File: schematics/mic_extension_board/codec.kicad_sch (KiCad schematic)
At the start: 26 parts, among them J10 Conn_01x01_Female, J11 Conn_01x01_Female, U6 CS4270-CZZ, X1 SG-5032CAN

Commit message: finished full board
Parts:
- C10, C12, C20: value 10uF -> C_Polarized
- C11, C13, C18, C21, C22: value 0.1uF -> C
- C14, C15: value 220pF -> C
- C16, C17: value 3.3uF -> C_Polarized
- C19: value 47uF -> C_Polarized
- C23, C24: value 3.3nF -> C
- R10, R9: value 470 -> R
- R19, R20: value 2k2 -> R
- R6: value 47k -> R
- R7, R8: value 10k -> R
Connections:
- net 3V3: now reaches C11.1, C13.1, R19.2, R20.2, U6.5 (VD), U6.8 (VLC), X1.4 (VCC)
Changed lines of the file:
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@@
   (junction (at 83.82 97.79) (diameter 0) (color 0 0 0 0)
   )
+  (junction (at 86.36 39.37) (diameter 0) (color 0 0 0 0)
+  )
   (junction (at 102.87 74.93) (diameter 0) (color 0 0 0 0)
   )
@@
     (stroke (width 0) (type default))
   )
+  (wire (pts (xy 86.36 39.37) (xy 82.55 39.37))
+    (stroke (width 0) (type default))
+  )
   (wire (pts (xy 95.25 85.09) (xy 99.06 85.09))
     (stroke (width 0) (type default))
@@
     (stroke (width 0) (type default))
   )
-  (wire (pts (xy 97.79 39.37) (xy 82.55 39.37))
+  (wire (pts (xy 97.79 39.37) (xy 86.36 39.37))
     (stroke (width 0) (type default))
   )
@@
     (stroke (width 0) (type default))
   )
+  (wire (pts (xy 86.36 36.83) (xy 86.36 39.37))
+    (stroke (width 0) (type default))
+  )
   (wire (pts (xy 144.78 116.84) (xy 214.63 116.84))
     (stroke (width 0) (type default))
@@
   (wire (pts (xy 90.17 82.55) (xy 99.06 82.55))
     (stroke (width 0) (type default))
+  )
+  (global_label "3V3" (shape input) (at 86.36 36.83 90) (fields_autoplaced)
+    (effects (font (size 1.27 1.27)) (justify left))
+    (property "Intersheetrefs" "${INTERSHEET_REFS}" (at 86.36 30.3372 90)
+      (effects (font (size 1.27 1.27)) (justify left) hide)
+    )
   )
   (global_label "5V" (shape input) (at 186.69 114.3 0) (fields_autoplaced)
@@
       (effects (font (size 1.27 1.27)))
     )
-    (property "Value" "470" (at 203.2 49.53 90)
+    (property "Value" "R" (at 203.2 49.53 90)
       (effects (font (size 1.27 1.27)))
     )
@@
       (effects (font (size 1.27 1.27)))
     )
-    (property "Value" "47uF" (at 191.77 92.71 90)
+    (property "Value" "C_Polarized" (at 191.77 92.71 90)
       (effects (font (size 1.27 1.27)))
     )
@@
       (effects (font (size 1.27 1.27)))
     )
-    (property "Value" "220pF" (at 111.76 97.79 90)
+    (property "Value" "C" (at 111.76 97.79 90)
       (effects (font (size 1.27 1.27)))
     )
@@
       (effects (font (size 1.27 1.27)))
     )
-    (property "Value" "10k" (at 191.77 52.07 90)
+    (property "Value" "R" (at 191.77 52.07 90)
       (effects (font (size 1.27 1.27)))
     )
@@
       (effects (font (size 1.27 1.27)))
     )
-    (property "Value" "3.3nF" (at 209.55 54.61 90)
+    (property "Value" "C" (at 209.55 54.61 90)
       (effects (font (size 1.27 1.27)))
     )
@@
       (effects (font (size 1.27 1.27)))
     )
-    (property "Value" "0.1uF" (at 189.23 102.87 90)
+    (property "Value" "C" (at 189.23 102.87 90)
       (effects (font (size 1.27 1.27)))
     )
@@
       (effects (font (size 1.27 1.27)))
     )
-    (property "Value" "3.3uF" (at 181.61 48.26 90)
+    (property "Value" "C_Polarized" (at 181.61 48.26 90)
       (effects (font (size 1.27 1.27)))
     )
@@
       (effects (font (size 1.27 1.27)))
     )
-    (property "Value" "2k2" (at 111.76 114.3 90)
+    (property "Value" "R" (at 111.76 114.3 90)
       (effects (font (size 1.27 1.27)))
     )
@@
       (effects (font (size 1.27 1.27)))
     )
-    (property "Value" "0.1uF" (at 207.01 88.9 90)
+    (property "Value" "C" (at 207.01 88.9 90)
       (effects (font (size 1.27 1.27)))
     )
@@
       (effects (font (size 1.27 1.27)))
     )
-    (property "Value" "10uF" (at 101.6 91.44 90)
+    (property "Value" "C_Polarized" (at 101.6 91.44 90)
       (effects (font (size 1.27 1.27)))
     )
@@
       (effects (font (size 1.27 1.27)))
     )
-    (property "Value" "0.1uF" (at 95.25 76.2 0)
+    (property "Value" "C" (at 95.25 76.2 0)
       (effects (font (size 1.27 1.27)))
     )
@@
       (effects (font (size 1.27 1.27)))
     )
-    (property "Value" "0.1uF" (at 207.01 96.52 90)
+    (property "Value" "C" (at 207.01 96.52 90)
       (effects (font (size 1.27 1.27)))
     )
@@
       (effects (font (size 1.27 1.27)))
     )
-    (property "Value" "10uF" (at 92.71 96.52 90)
+    (property "Value" "C_Polarized" (at 92.71 96.52 90)
       (effects (font (size 1.27 1.27)))
     )
@@
       (effects (font (size 1.27 1.27)))
     )
-    (property "Value" "10k" (at 194.31 67.31 90)
+    (property "Value" "R" (at 194.31 67.31 90)
       (effects (font (size 1.27 1.27)))
     )
@@
       (effects (font (size 1.27 1.27)))
     )
-    (property "Value" "0.1uF" (at 86.36 76.2 0)
+    (property "Value" "C" (at 86.36 76.2 0)
       (effects (font (size 1.27 1.27)))
     )
@@
       (effects (font (size 1.27 1.27)))
     )
-    (property "Value" "2k2" (at 111.76 118.11 90)
+    (property "Value" "R" (at 111.76 118.11 90)
       (effects (font (size 1.27 1.27)))
     )
@@
       (effects (font (size 1.27 1.27)))
     )
-    (property "Value" "3.3nF" (at 212.09 69.85 90)
+    (property "Value" "C" (at 212.09 69.85 90)
       (effects (font (size 1.27 1.27)))
     )
@@
       (effects (font (size 1.27 1.27)))
     )
-    (property "Value" "47k" (at 81.28 95.25 0)
+    (property "Value" "R" (at 81.28 95.25 0)
       (effects (font (size 1.27 1.27)))
     )
@@
       (effects (font (size 1.27 1.27)))
     )
-    (property "Value" "470" (at 205.74 64.77 90)
+    (property "Value" "R" (at 205.74 64.77 90)
       (effects (font (size 1.27 1.27)))
     )
@@
       (effects (font (size 1.27 1.27)))
     )
-    (property "Value" "10uF" (at 191.77 97.79 90)
+    (property "Value" "C_Polarized" (at 191.77 97.79 90)
       (effects (font (size 1.27 1.27)))
     )
@@
       (effects (font (size 1.27 1.27)))
     )
-    (property "Value" "3.3uF" (at 184.15 63.5 90)
+    (property "Value" "C_Polarized" (at 184.15 63.5 90)
       (effects (font (size 1.27 1.27)))
     )
@@
       (effects (font (size 1.27 1.27)))
     )
-    (property "Value" "220pF" (at 105.41 97.79 90)
-      (effects (font (size 1.27 1.27)))
-    )
+    (property "Value" "C" (at 105.41 97.79 90)
+      (effects (font (size 1.27 1.27)))
+    )

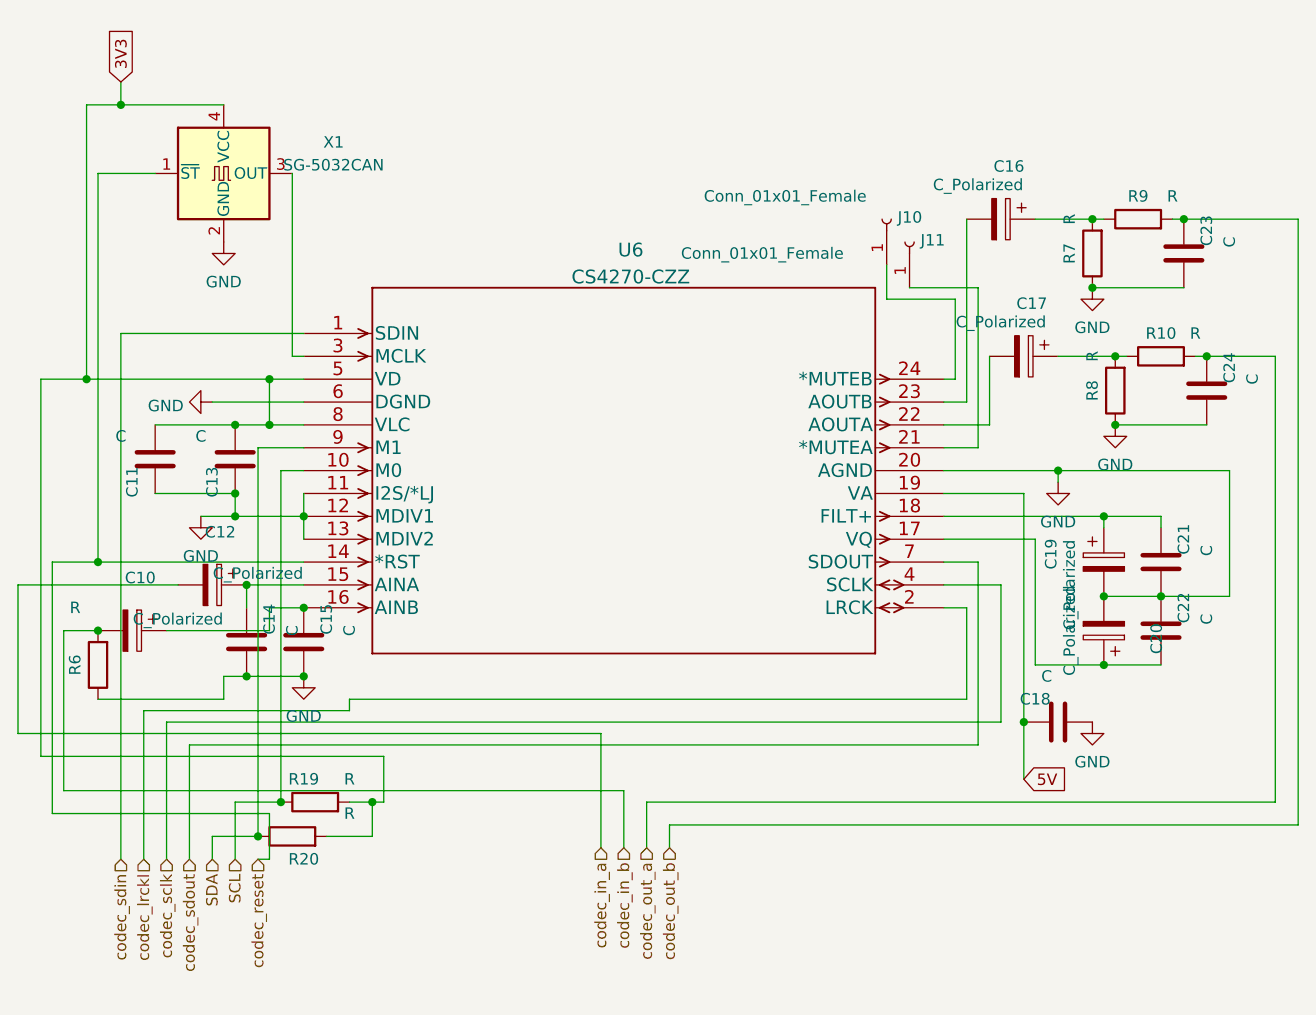
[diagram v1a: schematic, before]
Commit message: re-added component values previously lost due to kicad mishap
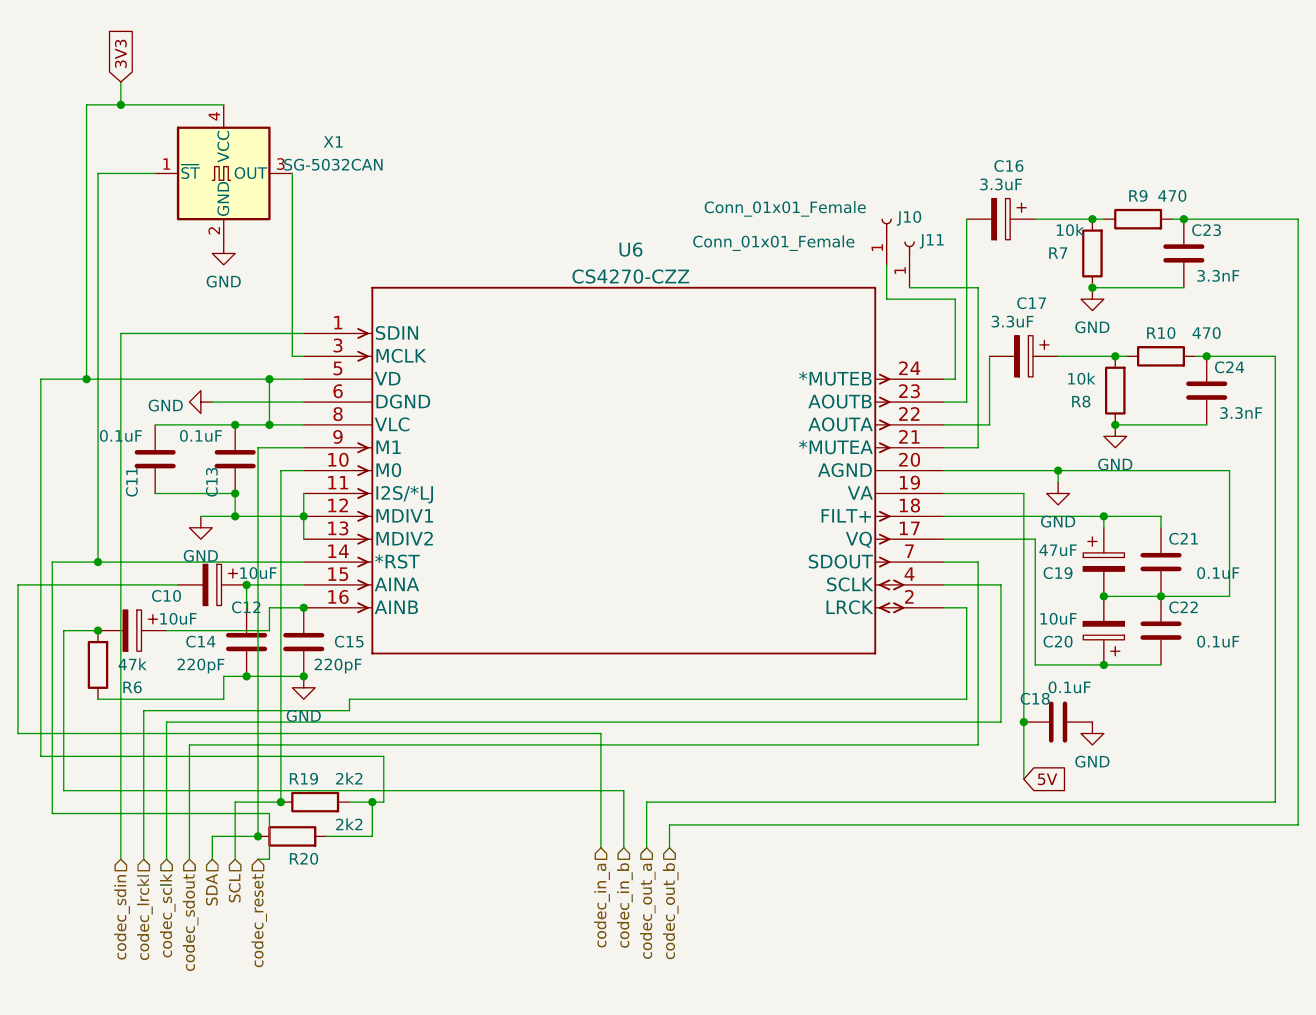
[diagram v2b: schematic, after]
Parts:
- C10, C12, C20: value C_Polarized -> 10uF
- C11, C13, C18, C21, C22: value C -> 0.1uF
- C14, C15: value C -> 220pF
- C16, C17: value C_Polarized -> 3.3uF
- C19: value C_Polarized -> 47uF
- C23, C24: value C -> 3.3nF
- R10, R9: value R -> 470
- R19, R20: value R -> 2k2
- R6: value R -> 47k
- R7, R8: value R -> 10k
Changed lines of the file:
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@@
       (effects (font (size 1.27 1.27)))
     )
-    (property "Value" "R" (at 203.2 49.53 90)
+    (property "Value" "470" (at 203.2 49.53 90)
       (effects (font (size 1.27 1.27)))
     )
@@
   (symbol (lib_id "Device:C_Polarized") (at 195.58 90.17 0) (unit 1)
     (in_bom yes) (on_board yes) (dnp no)
-    (property "Reference" "C19" (at 189.7212 89.281 90)
-      (effects (font (size 1.27 1.27)))
-    )
-    (property "Value" "C_Polarized" (at 191.77 92.71 90)
+    (property "Reference" "C19" (at 190.5 91.44 0)
+      (effects (font (size 1.27 1.27)))
+    )
+    (property "Value" "47uF" (at 190.5 88.9 0)
       (effects (font (size 1.27 1.27)))
     )
@@
   (symbol (lib_id "Device:C") (at 106.68 99.06 180) (unit 1)
     (in_bom yes) (on_board yes) (dnp no)
-    (property "Reference" "C15" (at 109.22 96.52 90)
-      (effects (font (size 1.27 1.27)))
-    )
-    (property "Value" "C" (at 111.76 97.79 90)
+    (property "Reference" "C15" (at 111.76 99.06 0)
+      (effects (font (size 1.27 1.27)))
+    )
+    (property "Value" "220pF" (at 110.49 101.6 0)
       (effects (font (size 1.27 1.27)))
     )
@@
   (symbol (lib_id "Device:R") (at 194.31 55.88 180) (unit 1)
     (in_bom yes) (on_board yes) (dnp no)
-    (property "Reference" "R7" (at 191.77 55.88 90)
-      (effects (font (size 1.27 1.27)))
-    )
-    (property "Value" "R" (at 191.77 52.07 90)
+    (property "Reference" "R7" (at 190.5 55.88 0)
+      (effects (font (size 1.27 1.27)))
+    )
+    (property "Value" "10k" (at 191.77 53.34 0)
       (effects (font (size 1.27 1.27)))
     )
@@
   (symbol (lib_id "Device:C") (at 204.47 55.88 180) (unit 1)
     (in_bom yes) (on_board yes) (dnp no)
-    (property "Reference" "C23" (at 207.01 53.34 90)
-      (effects (font (size 1.27 1.27)))
-    )
-    (property "Value" "C" (at 209.55 54.61 90)
+    (property "Reference" "C23" (at 207.01 53.34 0)
+      (effects (font (size 1.27 1.27)))
+    )
+    (property "Value" "3.3nF" (at 208.28 58.42 0)
       (effects (font (size 1.27 1.27)))
     )
@@
       (effects (font (size 1.27 1.27)))
     )
-    (property "Value" "C" (at 189.23 102.87 90)
+    (property "Value" "0.1uF" (at 191.77 104.14 90)
       (effects (font (size 1.27 1.27)))
     )
@@
       (effects (font (size 1.27 1.27)) (justify right))
     )
-    (property "Value" "Conn_01x01_Female" (at 151.13 49.53 90)
+    (property "Value" "Conn_01x01_Female" (at 151.13 50.8 90)
       (effects (font (size 1.27 1.27)) (justify right))
     )
@@
       (effects (font (size 1.27 1.27)))
     )
-    (property "Value" "C_Polarized" (at 181.61 48.26 90)
+    (property "Value" "3.3uF" (at 184.15 48.26 90)
       (effects (font (size 1.27 1.27)))
     )
@@
       (effects (font (size 1.27 1.27)))
     )
-    (property "Value" "R" (at 111.76 114.3 90)
+    (property "Value" "2k2" (at 111.76 114.3 90)
       (effects (font (size 1.27 1.27)))
     )
@@
   (symbol (lib_id "Device:C") (at 201.93 90.17 180) (unit 1)
     (in_bom yes) (on_board yes) (dnp no)
-    (property "Reference" "C21" (at 204.47 87.63 90)
-      (effects (font (size 1.27 1.27)))
-    )
-    (property "Value" "C" (at 207.01 88.9 90)
+    (property "Reference" "C21" (at 204.47 87.63 0)
+      (effects (font (size 1.27 1.27)))
+    )
+    (property "Value" "0.1uF" (at 208.28 91.44 0)
       (effects (font (size 1.27 1.27)))
     )
@@
   (symbol (lib_id "Device:C_Polarized") (at 96.52 92.71 270) (unit 1)
     (in_bom yes) (on_board yes) (dnp no)
-    (property "Reference" "C12" (at 97.409 86.8512 90)
-      (effects (font (size 1.27 1.27)))
-    )
-    (property "Value" "C_Polarized" (at 101.6 91.44 90)
+    (property "Reference" "C12" (at 100.33 95.25 90)
+      (effects (font (size 1.27 1.27)))
+    )
+    (property "Value" "10uF" (at 101.6 91.44 90)
       (effects (font (size 1.27 1.27)))
     )
@@
       (effects (font (size 1.27 1.27)))
     )
-    (property "Value" "C" (at 95.25 76.2 0)
+    (property "Value" "0.1uF" (at 95.25 76.2 0)
       (effects (font (size 1.27 1.27)))
     )
@@
   (symbol (lib_id "Device:C") (at 201.93 97.79 180) (unit 1)
     (in_bom yes) (on_board yes) (dnp no)
-    (property "Reference" "C22" (at 204.47 95.25 90)
-      (effects (font (size 1.27 1.27)))
-    )
-    (property "Value" "C" (at 207.01 96.52 90)
+    (property "Reference" "C22" (at 204.47 95.25 0)
+      (effects (font (size 1.27 1.27)))
+    )
+    (property "Value" "0.1uF" (at 208.28 99.06 0)
       (effects (font (size 1.27 1.27)))
     )
@@
   (symbol (lib_id "Device:C_Polarized") (at 87.63 97.79 270) (unit 1)
     (in_bom yes) (on_board yes) (dnp no)
-    (property "Reference" "C10" (at 88.519 91.9312 90)
-      (effects (font (size 1.27 1.27)))
-    )
-    (property "Value" "C_Polarized" (at 92.71 96.52 90)
+    (property "Reference" "C10" (at 91.44 93.98 90)
+      (effects (font (size 1.27 1.27)))
+    )
+    (property "Value" "10uF" (at 92.71 96.52 90)
       (effects (font (size 1.27 1.27)))
     )
@@
   (symbol (lib_id "Device:R") (at 196.85 71.12 180) (unit 1)
     (in_bom yes) (on_board yes) (dnp no)
-    (property "Reference" "R8" (at 194.31 71.12 90)
-      (effects (font (size 1.27 1.27)))
-    )
-    (property "Value" "R" (at 194.31 67.31 90)
+    (property "Reference" "R8" (at 193.04 72.39 0)
+      (effects (font (size 1.27 1.27)))
+    )
+    (property "Value" "10k" (at 193.04 69.85 0)
       (effects (font (size 1.27 1.27)))
     )
@@
       (effects (font (size 1.27 1.27)))
     )
-    (property "Value" "C" (at 86.36 76.2 0)
+    (property "Value" "0.1uF" (at 86.36 76.2 0)
       (effects (font (size 1.27 1.27)))
     )
@@
       (effects (font (size 1.27 1.27)))
     )
-    (property "Value" "R" (at 111.76 118.11 90)
+    (property "Value" "2k2" (at 111.76 119.38 90)
       (effects (font (size 1.27 1.27)))
     )
@@
   (symbol (lib_id "Device:C") (at 207.01 71.12 180) (unit 1)
     (in_bom yes) (on_board yes) (dnp no)
-    (property "Reference" "C24" (at 209.55 68.58 90)
-      (effects (font (size 1.27 1.27)))
-    )
-    (property "Value" "C" (at 212.09 69.85 90)
+    (property "Reference" "C24" (at 209.55 68.58 0)
+      (effects (font (size 1.27 1.27)))
+    )
+    (property "Value" "3.3nF" (at 210.82 73.66 0)
       (effects (font (size 1.27 1.27)))
     )
@@
   (symbol (lib_id "Device:R") (at 83.82 101.6 180) (unit 1)
     (in_bom yes) (on_board yes) (dnp no)
-    (property "Reference" "R6" (at 81.28 101.6 90)
-      (effects (font (size 1.27 1.27)))
-    )
-    (property "Value" "R" (at 81.28 95.25 0)
+    (property "Reference" "R6" (at 87.63 104.14 0)
+      (effects (font (size 1.27 1.27)))
+    )
+    (property "Value" "47k" (at 87.63 101.6 0)
       (effects (font (size 1.27 1.27)))
     )
@@
       (effects (font (size 1.27 1.27)) (justify right))
     )
-    (property "Value" "Conn_01x01_Female" (at 148.59 55.88 90)
+    (property "Value" "Conn_01x01_Female" (at 149.86 54.61 90)
       (effects (font (size 1.27 1.27)) (justify right))
     )
@@
       (effects (font (size 1.27 1.27)))
     )
-    (property "Value" "R" (at 205.74 64.77 90)
+    (property "Value" "470" (at 207.01 64.77 90)
       (effects (font (size 1.27 1.27)))
     )
@@
   (symbol (lib_id "Device:C_Polarized") (at 195.58 97.79 180) (unit 1)
     (in_bom yes) (on_board yes) (dnp no)
-    (property "Reference" "C20" (at 201.4388 98.679 90)
-      (effects (font (size 1.27 1.27)))
-    )
-    (property "Value" "C_Polarized" (at 191.77 97.79 90)
+    (property "Reference" "C20" (at 190.5 99.06 0)
+      (effects (font (size 1.27 1.27)))
+    )
+    (property "Value" "10uF" (at 190.5 96.52 0)
       (effects (font (size 1.27 1.27)))
     )
@@
       (effects (font (size 1.27 1.27)))
     )
-    (property "Value" "C_Polarized" (at 184.15 63.5 90)
+    (property "Value" "3.3uF" (at 185.42 63.5 90)
       (effects (font (size 1.27 1.27)))
     )
@@
   (symbol (lib_id "Device:C") (at 100.33 99.06 180) (unit 1)
     (in_bom yes) (on_board yes) (dnp no)
-    (property "Reference" "C14" (at 102.87 96.52 90)
-      (effects (font (size 1.27 1.27)))
-    )
-    (property "Value" "C" (at 105.41 97.79 90)
-      (effects (font (size 1.27 1.27)))
-    )
+    (property "Reference" "C14" (at 95.25 99.06 0)
+      (effects (font (size 1.27 1.27)))
+    )
+    (property "Value" "220pF" (at 95.25 101.6 0)
+      (effects (font (size 1.27 1.27)))
+    )
